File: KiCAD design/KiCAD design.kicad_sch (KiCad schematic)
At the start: 0 parts

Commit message: correction of errors
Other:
- sheet CONNECTORS ports: added BATT, CURRENT_MEASURE, LED1, LED2; removed none
- sheet ON_BOARD_COMPONENTS ports: added CURRENT_MEASURE, IP+, LED1, LED2; removed none
- sheet POWER_SUPPLY ports: added BATT, IP+; removed none

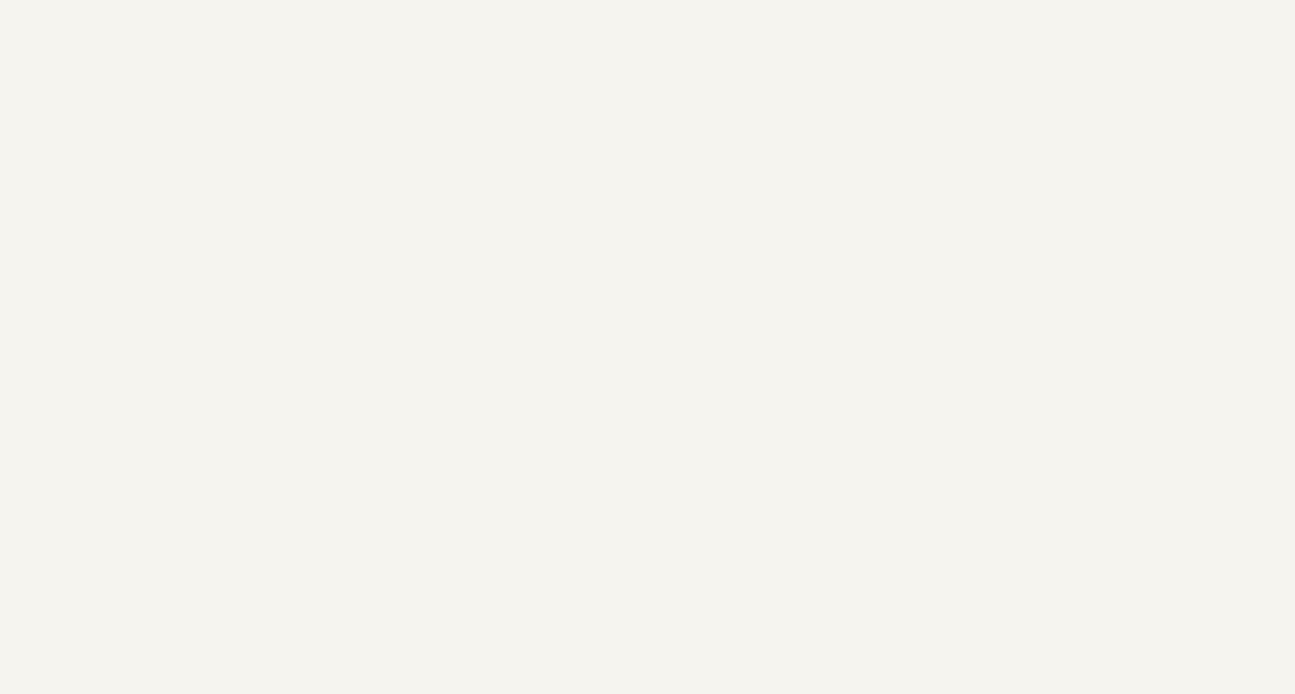
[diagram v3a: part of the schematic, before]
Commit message: add of footprint and nucleo as a reference
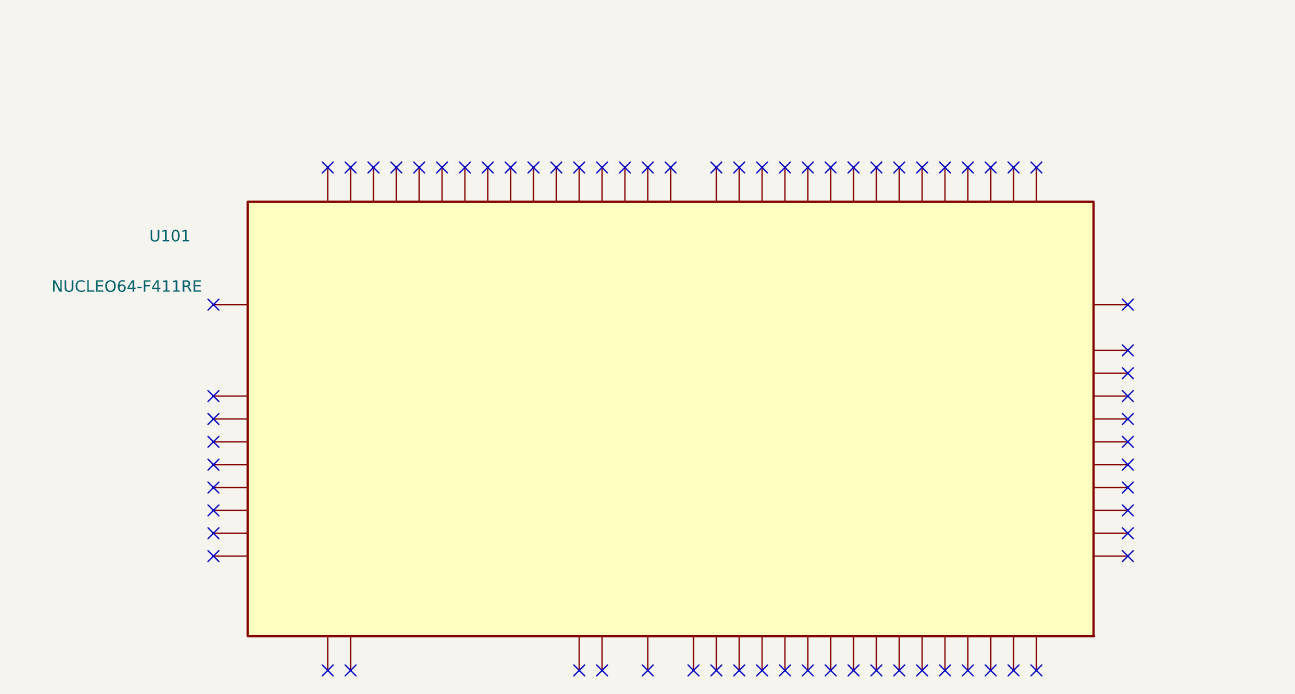
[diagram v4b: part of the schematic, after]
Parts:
- added U101: NUCLEO64-F411RE, Module:ST_Morpho_Connector_144_STLink, symbol MCU_Module:NUCLEO64-F411RE
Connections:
- no-connect marks 0 -> 72
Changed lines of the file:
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@@
 (kicad_sch (version 20211123) (generator eeschema)
   (paper "A4")
+  (no_connect (at 73.66 121.92))
+  (no_connect (at 119.38 121.92))
+  (no_connect (at 127 177.8))
+  (no_connect (at 66.04 121.92))
+  (no_connect (at 119.38 177.8))
+  (no_connect (at 43.18 152.4))
+  (no_connect (at 111.76 121.92))
+  (no_connect (at 96.52 177.8))
+  (no_connect (at 109.22 121.92))
+  (no_connect (at 78.74 121.92))
+  (no_connect (at 116.84 121.92))
+  (no_connect (at 134.62 121.92))
+  (no_connect (at 43.18 160.02))
+  (no_connect (at 101.6 177.8))
+  (no_connect (at 144.78 137.16))
+  (no_connect (at 60.96 121.92))
+  (no_connect (at 127 121.92))
+  (no_connect (at 43.18 154.94))
+  (no_connect (at 55.88 121.92))
+  (no_connect (at 43.18 165.1))
+  (no_connect (at 132.08 177.8))
+  (no_connect (at 144.78 165.1))
+  (no_connect (at 43.18 149.86))
+  (no_connect (at 111.76 177.8))
+  (no_connect (at 71.12 121.92))
+  (no_connect (at 68.58 121.92))
+  (no_connect (at 43.18 147.32))
+  (no_connect (at 58.42 177.8))
+  (no_connect (at 91.44 177.8))
+  (no_connect (at 55.88 177.8))
+  (no_connect (at 91.44 121.92))
+  (no_connect (at 129.54 121.92))
+  (no_connect (at 43.18 137.16))
+  (no_connect (at 129.54 177.8))
+  (no_connect (at 144.78 157.48))
+  (no_connect (at 106.68 177.8))
+  (no_connect (at 106.68 121.92))
+  (no_connect (at 124.46 121.92))
+  (no_connect (at 144.78 154.94))
+  (no_connect (at 99.06 121.92))
+  (no_connect (at 101.6 121.92))
+  (no_connect (at 144.78 144.78))
+  (no_connect (at 114.3 177.8))
+  (no_connect (at 86.36 121.92))
+  (no_connect (at 63.5 121.92))
+  (no_connect (at 144.78 142.24))
+  (no_connect (at 144.78 147.32))
+  (no_connect (at 124.46 177.8))
+  (no_connect (at 83.82 121.92))
+  (no_connect (at 144.78 160.02))
+  (no_connect (at 86.36 177.8))
+  (no_connect (at 144.78 149.86))
+  (no_connect (at 132.08 121.92))
+  (no_connect (at 83.82 177.8))
+  (no_connect (at 144.78 152.4))
+  (no_connect (at 81.28 121.92))
+  (no_connect (at 109.22 177.8))
+  (no_connect (at 99.06 177.8))
+  (no_connect (at 58.42 121.92))
+  (no_connect (at 121.92 121.92))
+  (no_connect (at 121.92 177.8))
+  (no_connect (at 43.18 162.56))
+  (no_connect (at 116.84 177.8))
+  (no_connect (at 114.3 121.92))
+  (no_connect (at 144.78 162.56))
+  (no_connect (at 88.9 121.92))
+  (no_connect (at 93.98 121.92))
+  (no_connect (at 104.14 177.8))
+  (no_connect (at 76.2 121.92))
+  (no_connect (at 134.62 177.8))
+  (no_connect (at 43.18 157.48))
+  (no_connect (at 104.14 121.92))
   (wire (pts (xy 177.8 38.1) (xy 208.28 38.1))
     (stroke (width 0) (type default) (color 0 0 0 0))
@@
   (wire (pts (xy 73.66 68.58) (xy 119.38 68.58))
     (stroke (width 0) (type default) (color 0 0 0 0))
+  )
+  (symbol (lib_id "MCU_Module:NUCLEO64-F411RE") (at 93.98 149.86 90) (unit 1)
+    (in_bom no) (on_board yes)
+    (property "Reference" "U101" (id 0) (at 40.64 129.54 90)
+      (effects (font (size 1.27 1.27)) (justify left))
+    )
+    (property "Value" "NUCLEO64-F411RE" (id 1) (at 41.91 135.1406 90)
+      (effects (font (size 1.27 1.27)) (justify left))
+    )
+    (property "Footprint" "Module:ST_Morpho_Connector_144_STLink" (id 2) (at 44.45 135.1406 0)
+      (effects (font (size 1.27 1.27)) (justify left) hide)
+    )
+    (property "Datasheet" "http://www.st.com/st-web-ui/static/active/en/resource/technical/document/data_brief/DM00105918.pdf" (id 3) (at 129.54 172.72 0)
+      (effects (font (size 1.27 1.27)) hide)
+    )
+    (pin "1")
+    (pin "10")
+    (pin "11")
+    (pin "12")
+    (pin "13")
+    (pin "14")
+    (pin "15")
+    (pin "16")
+    (pin "17")
+    (pin "18")
+    (pin "19")
+    (pin "2")
+    (pin "20")
+    (pin "21")
+    (pin "22")
+    (pin "23")
+    (pin "24")
+    (pin "25")
+    (pin "26")
+    (pin "27")
+    (pin "28")
+    (pin "29")
+    (pin "3")
+    (pin "30")
+    (pin "31")
+    (pin "32")
+    (pin "33")
+    (pin "34")
+    (pin "35")
+    (pin "36")
+    (pin "37")
+    (pin "38")
+    (pin "39")
+    (pin "4")
+    (pin "40")
+    (pin "41")
+    (pin "42")
+    (pin "43")
+    (pin "44")
+    (pin "45")
+    (pin "46")
+    (pin "47")
+    (pin "48")
+    (pin "49")
+    (pin "5")
+    (pin "50")
+    (pin "51")
+    (pin "52")
+    (pin "53")
+    (pin "54")
+    (pin "55")
+    (pin "56")
+    (pin "57")
+    (pin "58")
+    (pin "59")
+    (pin "6")
+    (pin "60")
+    (pin "61")
+    (pin "62")
+    (pin "63")
+    (pin "64")
+    (pin "65")
+    (pin "66")
+    (pin "67")
+    (pin "68")
+    (pin "69")
+    (pin "7")
+    (pin "70")
+    (pin "71")
+    (pin "72")
+    (pin "73")
+    (pin "74")
+    (pin "75")
+    (pin "76")
+    (pin "77")
+    (pin "78")
+    (pin "79")
+    (pin "8")
+    (pin "80")
+    (pin "9")
   )
   (sheet (at 127 25.4) (size 50.8 50.8) (fields_autoplaced)
@@
     )
     (path "/3203fe18-fa26-4a56-94ee-1c822c5de1df/258b6a41-8709-4213-942d-4b29ad5265c0"
-      (reference "C401") (unit 1) (value "0.1uF") (footprint "")
+      (reference "C401") (unit 1) (value "0.1uF") (footprint "Capacitor_SMD:C_0603_1608Metric_Pad1.08x0.95mm_HandSolder")
     )
     (path "/3203fe18-fa26-4a56-94ee-1c822c5de1df/457d9f27-6ce4-46f7-9775-a072cf15db80"
-      (reference "C402") (unit 1) (value "1nF") (footprint "")
+      (reference "C402") (unit 1) (value "1nF") (footprint "Capacitor_SMD:C_0603_1608Metric_Pad1.08x0.95mm_HandSolder")
     )
     (path "/3203fe18-fa26-4a56-94ee-1c822c5de1df/6cd77127-9612-46e2-8a8a-cbbf962ef9f1"
@@
     )
     (path "/351b992e-9d0c-41fd-a6c4-f130ac0d9617/73cd9a15-3818-472e-a397-2c2e429393a2"
-      (reference "J201") (unit 1) (value "Conn_02x19_Odd_Even") (footprint "")
+      (reference "J201") (unit 1) (value "Conn_02x19_Odd_Even") (footprint "Connector_JST:JST_PUD_B38B-PUDSS_2x19_P2.00mm_Vertical")
     )
     (path "/351b992e-9d0c-41fd-a6c4-f130ac0d9617/aa640231-ba2c-4b56-80ae-30c2b8ca8433"
-      (reference "J202") (unit 1) (value "Conn_01x03_Female") (footprint "")
+      (reference "J202") (unit 1) (value "Conn_01x03_Female") (footprint "Connector_JST:JST_XH_B3B-XH-A_1x03_P2.50mm_Vertical")
     )
     (path "/351b992e-9d0c-41fd-a6c4-f130ac0d9617/19a72238-6ca2-485e-a43e-53fa5deb8112"
-      (reference "J203") (unit 1) (value "Conn_01x03_Female") (footprint "")
+      (reference "J203") (unit 1) (value "Conn_01x03_Female") (footprint "Connector_JST:JST_XH_B3B-XH-A_1x03_P2.50mm_Vertical")
     )
     (path "/351b992e-9d0c-41fd-a6c4-f130ac0d9617/61b8790e-0f11-47f3-abae-cb6881888e1b"
-      (reference "J204") (unit 1) (value "Conn_02x19_Odd_Even") (footprint "")
+      (reference "J204") (unit 1) (value "Conn_02x19_Odd_Even") (footprint "Connector_JST:JST_PUD_B38B-PUDSS_2x19_P2.00mm_Vertical")
     )
     (path "/351b992e-9d0c-41fd-a6c4-f130ac0d9617/96e895de-633b-4f92-b3ff-7845046ea630"
@@
     )
     (path "/351b992e-9d0c-41fd-a6c4-f130ac0d9617/fdd55bf3-8721-430d-b756-5f86881de1a0"
-      (reference "J207") (unit 1) (value "Conn_01x06_Female") (footprint "")
+      (reference "J207") (unit 1) (value "Conn_01x06_Female") (footprint "Connector_JST:JST_XH_B6B-XH-A_1x06_P2.50mm_Vertical")
     )
     (path "/351b992e-9d0c-41fd-a6c4-f130ac0d9617/77ef5647-5fd0-45a7-8f1c-57b486318a65"
@@
       (reference "SW301") (unit 1) (value "~") (footprint "composants_projet_footprint:1A11-NF5STSE-B")
     )
+    (path "/53ab80cb-680d-47b5-9042-b10ff93ac434"
+      (reference "U101") (unit 1) (value "NUCLEO64-F411RE") (footprint "Module:ST_Morpho_Connector_144_STLink")
+    )
     (path "/465a2d22-51a7-48d6-b1e0-fc75f581e914/9480c12b-095c-4fc3-a989-57ee26360abb"

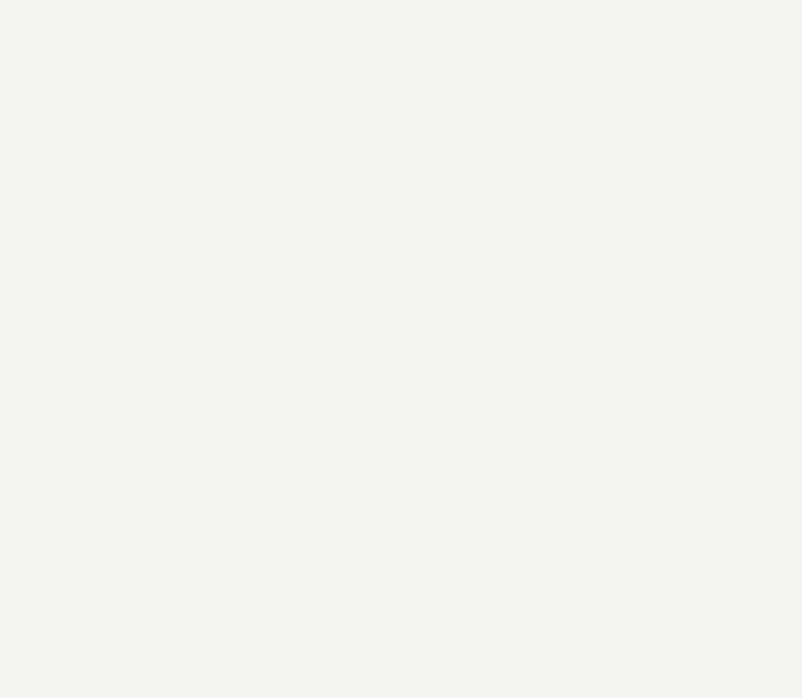
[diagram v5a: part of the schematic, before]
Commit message: add purchase location (field PurchaseLoc) and price (field Price) to some main components, adding rest later
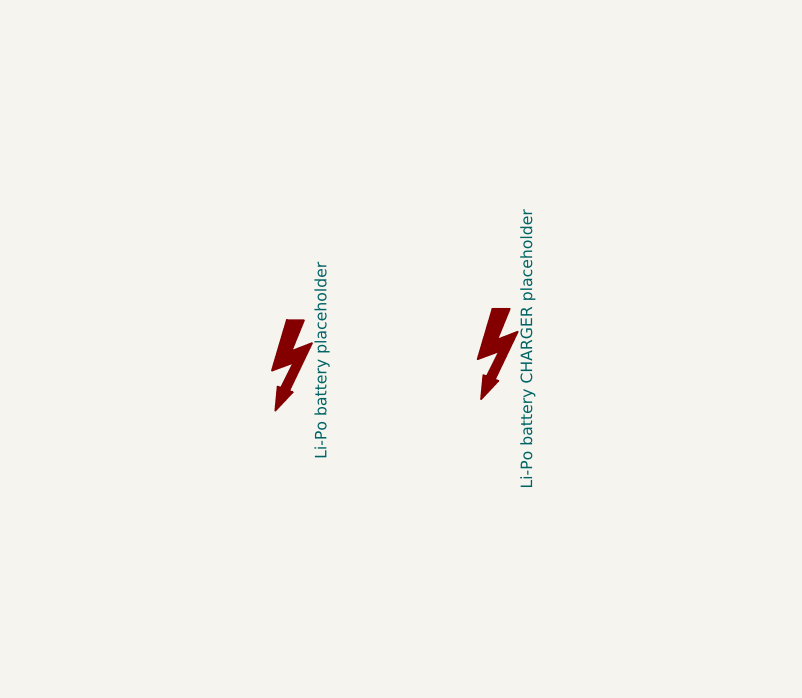
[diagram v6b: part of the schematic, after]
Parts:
- added LiPo_bat401: Li-Po battery placeholder, symbol Graphic:SYM_Flash_Large
- added LiPo_charger401: Li-Po battery CHARGER placeholder, symbol Graphic:SYM_Flash_Large
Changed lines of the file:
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@@
     (stroke (width 0) (type default) (color 0 0 0 0))
+  )
+  (symbol (lib_id "Graphic:SYM_Flash_Large") (at 207.01 127 0) (unit 1)
+    (in_bom yes) (on_board yes) (fields_autoplaced)
+    (property "Reference" "LiPo_bat401" (id 0) (at 203.2 127 90)
+      (effects (font (size 1.27 1.27)) hide)
+    )
+    (property "Value" "Li-Po battery placeholder" (id 1) (at 210.312 127 90))
+    (property "Footprint" "" (id 2) (at 206.756 129.286 0)
+      (effects (font (size 1.27 1.27)) hide)
+    )
+    (property "Datasheet" "~" (id 3) (at 217.17 129.54 0)
+      (effects (font (size 1.27 1.27)) hide)
+    )
+    (property "PurchaseLoc" "https://hobbyking.com/en_us/zippy-compact-1800mah-3s-25c-lipo-pack.html" (id 4) (at 207.01 127 90)
+      (effects (font (size 1.27 1.27)) hide)
+    )
+    (property "Price" "13.42" (id 5) (at 207.01 127 90)
+      (effects (font (size 1.27 1.27)) hide)
+    )
+  )
+  (symbol (lib_id "Graphic:SYM_Flash_Large") (at 229.87 125.73 0) (unit 1)
+    (in_bom yes) (on_board yes) (fields_autoplaced)
+    (property "Reference" "LiPo_charger401" (id 0) (at 226.06 125.73 90)
+      (effects (font (size 1.27 1.27)) hide)
+    )
+    (property "Value" "Li-Po battery CHARGER placeholder" (id 1) (at 233.172 125.73 90))
+    (property "Footprint" "" (id 2) (at 229.616 128.016 0)
+      (effects (font (size 1.27 1.27)) hide)
+    )
+    (property "Datasheet" "~" (id 3) (at 240.03 128.27 0)
+      (effects (font (size 1.27 1.27)) hide)
+    )
+    (property "PurchaseLoc" "https://hobbyking.com/en_us/turnigy-e3-compact-2s-3s-lipo-charger-100-240v-eu-plug.html" (id 4) (at 229.87 125.73 90)
+      (effects (font (size 1.27 1.27)) hide)
+    )
+    (property "Price" "14.39" (id 5) (at 229.87 125.73 90)
+      (effects (font (size 1.27 1.27)) hide)
+    )
   )
   (symbol (lib_id "MCU_Module:NUCLEO64-F411RE") (at 93.98 149.86 90) (unit 1)
@@
       (reference "J208") (unit 1) (value "JST SENS TOF 1") (footprint "Connector_JST:JST_XH_B6B-XH-A_1x06_P2.50mm_Vertical")
     )
+    (path "/11dd6d81-7255-48cc-8812-0f9f86181d16"
+      (reference "LiPo_bat401") (unit 1) (value "Li-Po battery placeholder") (footprint "")
+    )
+    (path "/300626cb-8874-43dc-8300-c3f8e2249cd7"
+      (reference "LiPo_charger401") (unit 1) (value "Li-Po battery CHARGER placeholder") (footprint "")
+    )
     (path "/3203fe18-fa26-4a56-94ee-1c822c5de1df/babb38ec-e470-4f2b-ac32-e46727abe3d3"
